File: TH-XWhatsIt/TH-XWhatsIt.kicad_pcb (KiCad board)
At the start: 2 copper layers, 178 x 115.5 mm, 42 parts, among them J1 COLUMNS, J10 DISPLAYWRITER PLUGBOARD CONNE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, J11 DISPLAYWRITER PLUGBOARD ROWS, J12 EXPANSION HEADER, J2 ROWS, J3 MODEL F PLUGBOARD COLUMNS, J4 MODEL F PLUGBOARD CONNECTOR, J5 MODEL F PLUGBOARD ROWS, J6 BEAMSPRING PLUGBOARD COLUMNS, J7 BEAMSPRING PLUGBOARD CONNECTOR, J8 BEAMSPRING PLUGBOARD ROWS, J9 DISPLAYWRITER PLUGBOARD COLUM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, U1 LM339, U2 MCP4921-EP, U3 74HCT595, U5 74HCT595, U6 LM339, U7 ProMicro, U8 74HCT595

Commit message: My try of adding model-f at support
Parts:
- removed C2: 10U, Capacitor_THT:C_Disc_D3.0mm_W1.6mm_P2.50mm
- removed H2: GROUND STRAP, MountingHole:MountingHole_2.2mm_M2_Pad_Via
- removed J11: DISPLAYWRITER PLUGBOARD ROWS, Connector_PinSocket_2.54mm:PinSocket_1x12_P2.54mm_Vertical
- removed J4: MODEL F PLUGBOARD CONNECTOR, Connector_PinHeader_2.54mm:PinHeader_1x30_P2.54mm_Horizontal
- removed J5: MODEL F PLUGBOARD ROWS, Connector_PinSocket_2.54mm:PinSocket_1x12_P2.54mm_Vertical
- removed J6: BEAMSPRING PLUGBOARD COLUMNS, Connector_PinSocket_2.54mm:PinSocket_1x27_P2.54mm_Vertical
- removed J8: BEAMSPRING PLUGBOARD ROWS, Connector_PinSocket_2.54mm:PinSocket_1x12_P2.54mm_Vertical
- removed J9: DISPLAYWRITER PLUGBOARD COLUMNS, Connector_PinSocket_2.54mm:PinSocket_1x27_P2.54mm_Vertical
- removed R6: 4K7, Resistor_THT:R_Axial_DIN0204_L3.6mm_D1.6mm_P1.90mm_Vertical
- removed R7: 1K, Resistor_THT:R_Axial_DIN0204_L3.6mm_D1.6mm_P1.90mm_Vertical
- added H10: GROUND STRAP, MountingHole:MountingHole_4.5mm_Pad, F.Cu at (225.6, 149.3)
- added J13: Conn_01x30, TH-XWhatsIt:SIP-30-P3.96, F.Cu at (159.3, 150.2)
- added J22: Conn_01x08, Connector_PinSocket_2.54mm:PinSocket_1x08_P2.54mm_Vertical, F.Cu at (149.4, 139.1)
- added J44: MODEL F PLUGBOARD CONNECTOR, Connector_PinHeader_2.54mm:PinHeader_1x30_P2.54mm_Horizontal, B.Cu at (124.0, 146.1)
- H1, H3, H4: footprint MountingHole:MountingHole_2.2mm_M2_Pad_Via -> MountingHole:MountingHole_3.2mm_M3_Pad
- J1: value COLUMNS -> Conn_01x08; footprint Connector_PinHeader_2.54mm:PinHeader_1x27_P2.54mm_Vertical -> Connector_PinSocket_2.54mm:PinSocket_1x08_P2.54mm_Vertical; moved to B.Cu
- J2: value ROWS -> MODEL F PLUGBOARD CONNECTOR; footprint Connector_PinHeader_2.54mm:PinHeader_1x12_P2.54mm_Vertical -> Connector_PinHeader_2.54mm:PinHeader_1x30_P2.54mm_Vertical; moved to B.Cu
- J3: value MODEL F PLUGBOARD COLUMNS -> MODEL F PLUGBOARD CONNECTOR; footprint Connector_PinSocket_2.54mm:PinSocket_1x27_P2.54mm_Vertical -> Connector_PinHeader_2.54mm:PinHeader_1x30_P2.54mm_Vertical; moved to F.Cu
- moved J2 100.0 mm to (124.0, 116.7)
- moved J1 69.6 mm to (149.4, 109.1), turned to 270 degrees
- moved J3 44.4 mm to (123.9, 87.3), turned to 90 degrees
- moved R1 9.41 mm to (225.3, 133.7)
- moved RN3 8.68 mm to (198.1, 138.9), turned to 180 degrees
- moved C10 8.34 mm to (204.8, 124.6), turned to 180 degrees
- moved R2 7.66 mm to (228.0, 135.6), turned to 90 degrees
- moved RN1 7.66 mm to (217.2, 138.8)
- moved C4 5.85 mm to (166.7, 126.3)
- moved C3 5.69 mm to (166.7, 132.3)
- moved U2 5.58 mm to (170.6, 134.3)
- moved C7 5.45 mm to (136.8, 132.1)
- moved U8 5.39 mm to (140.4, 134.7)
- moved C5 5.38 mm to (111.7, 132.1)
- moved U3 5.37 mm to (90.2, 134.6)
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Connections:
- J1 pad 1: GNDA -> /beamspring plugboard/BSCOL17
- J1 pad 2: GNDA -> /beamspring plugboard/BSCOL18
- J1 pad 3: COL1 -> /beamspring plugboard/BSCOL19
- J1 pad 4: COL2 -> /beamspring plugboard/BSCOL20
- J1 pad 5: COL3 -> /beamspring plugboard/BSCOL21
- J1 pad 6: COL4 -> /beamspring plugboard/BSCOL22
- J1 pad 7: COL5 -> /beamspring plugboard/BSCOL23
- J1 pad 8: COL6 -> /beamspring plugboard/BSGROUND
- J2 pad 1: GNDA -> /beamspring plugboard/BSGROUND
- J2 pad 10: SENSE8 -> /beamspring plugboard/BSCOL8
- J2 pad 11: GNDA -> /beamspring plugboard/BSCOL9
- J2 pad 12: GNDA -> /beamspring plugboard/BSCOL10
- J2 pad 2: GNDA -> /beamspring plugboard/BSGROUND
- J2 pad 3: SENSE1 -> /beamspring plugboard/BSCOL1
- J2 pad 4: SENSE2 -> /beamspring plugboard/BSCOL2
- J2 pad 5: SENSE3 -> /beamspring plugboard/BSCOL3
- J2 pad 6: SENSE4 -> /beamspring plugboard/BSCOL4
- J2 pad 7: SENSE5 -> /beamspring plugboard/BSCOL5
- J2 pad 8: SENSE7 -> /beamspring plugboard/BSCOL6
- J2 pad 9: SENSE6 -> /beamspring plugboard/BSCOL7
- J3 pad 1: /model f plugboard/MFGROUND -> /displaywriter plugboard/DWGROUND
- J3 pad 10: /model f plugboard/MFCOL8 -> /displaywriter plugboard/DWCOL8
- J3 pad 11: /model f plugboard/MFCOL9 -> /displaywriter plugboard/DWCOL9
- J3 pad 12: /model f plugboard/MFCOL10 -> /displaywriter plugboard/DWCOL10
- J3 pad 13: /model f plugboard/MFCOL11 -> /displaywriter plugboard/DWCOL11
- J3 pad 14: /model f plugboard/MFCOL12 -> /displaywriter plugboard/DWCOL12
- J3 pad 15: /model f plugboard/MFCOL13 -> (no net)
- J3 pad 16: /model f plugboard/MFCOL14 -> (no net)
- J3 pad 17: /model f plugboard/MFCOL15 -> (no net)
- J3 pad 18: /model f plugboard/MFCOL16 -> (no net)
- J3 pad 19: (no net) -> /displaywriter plugboard/DWGROUND
- J3 pad 2: /model f plugboard/MFGROUND -> /displaywriter plugboard/DWGROUND
- J3 pad 20: (no net) -> /displaywriter plugboard/DWGROUND
- J3 pad 21: (no net) -> /displaywriter plugboard/DWSENSE1
- J3 pad 22: (no net) -> /displaywriter plugboard/DWSENSE2
- J3 pad 23: (no net) -> /displaywriter plugboard/DWSENSE3
- J3 pad 24: (no net) -> /displaywriter plugboard/DWSENSE4
- J3 pad 25: (no net) -> /displaywriter plugboard/DWSENSE8
- J3 pad 26: /model f plugboard/MFGROUND -> /displaywriter plugboard/DWSENSE7
- J3 pad 27: /model f plugboard/MFGROUND -> /displaywriter plugboard/DWSENSE6
- J3 pad 3: /model f plugboard/MFCOL1 -> /displaywriter plugboard/DWCOL1
- J3 pad 4: /model f plugboard/MFCOL2 -> /displaywriter plugboard/DWCOL2
- J3 pad 5: /model f plugboard/MFCOL3 -> /displaywriter plugboard/DWCOL3
- J3 pad 6: /model f plugboard/MFCOL4 -> /displaywriter plugboard/DWCOL4
- J3 pad 7: /model f plugboard/MFCOL5 -> /displaywriter plugboard/DWCOL5
- J3 pad 8: /model f plugboard/MFCOL6 -> /displaywriter plugboard/DWCOL6
- J3 pad 9: /model f plugboard/MFCOL7 -> /displaywriter plugboard/DWCOL7
- RN3 pad 1: Net-(R6-Pad2) -> Net-(R1-Pad2)
- RN3 pad 2: SENSE8 -> SENSE5
- RN3 pad 3: SENSE6 -> SENSE7
- RN3 pad 4: SENSE7 -> SENSE6
- RN3 pad 5: SENSE5 -> SENSE8
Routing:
- net /model f plugboard/MFGROUND: track 318.4 -> 0.00 mm
- net +5VA: track 517.5 -> 414.4 mm, vias 2 -> 0
- net COL1: track 18.9 -> 75.3 mm
- net COL2: track 9.81 -> 65.7 mm
- net COL3: track 9.25 -> 64.3 mm
- net COL4: track 9.25 -> 62.9 mm
- net COL5: track 9.25 -> 61.4 mm
- net /model f plugboard/MFSENSE1: track 52.1 -> 0.00 mm
- net /model f plugboard/MFSENSE8: track 51.1 -> 0.00 mm
- net /model f plugboard/MFSENSE6: track 51.1 -> 0.00 mm
- net /model f plugboard/MFSENSE3: track 51.1 -> 0.00 mm
- net /model f plugboard/MFSENSE7: track 51.1 -> 0.00 mm
- net /model f plugboard/MFSENSE5: track 51.1 -> 0.00 mm
- net /model f plugboard/MFSENSE4: track 51.1 -> 0.00 mm
- net /model f plugboard/MFSENSE2: track 51.1 -> 0.00 mm
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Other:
- board size 178 x 115.5 mm -> 178 x 93.7 mm

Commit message: move stuff around near sense lines
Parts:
- moved C10 23.2 mm to (186.9, 139.4), turned to 0 degrees
- moved C9 21.0 mm to (208.8, 139.5)
- moved RN1 4.69 mm to (221.9, 139.2)
- moved RN3 4.67 mm to (202.8, 139.0)
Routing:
- net GNDA: track 488.8 -> 459.9 mm, vias 5 -> 3
- net Net-(R1-Pad2): track 52.4 -> 59.6 mm, vias 2 -> 1
- net SENSE3: track 55.3 -> 58.4 mm
- net SENSE6: track 40.8 -> 43.8 mm
- net SETPOINT: track 87.5 -> 90.0 mm, vias 1 -> 0
- net SENSE4: track 52.8 -> 55.2 mm
- net SENSE8: track 38.4 -> 40.7 mm
- net SENSE2: track 47.6 -> 49.4 mm
- net SENSE7: track 33.1 -> 34.8 mm
- net SENSE1: track 52.7 -> 51.8 mm

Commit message: some more small fixes
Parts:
- J13: value Conn_01x30 -> Model F AT
- J22: value Conn_01x08 -> Beamsring extra
- J44: value MODEL F PLUGBOARD CONNECTOR -> Model F or Plugboard
- U7: footprint promicro:ProMicro -> TH-XWhatsIt:ProMicro
- moved C10 2.52 mm to (189.4, 139.4), turned to 180 degrees
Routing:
- net +5VA: track 414.5 -> 415.6 mm
- net GNDA: track 459.9 -> 459.6 mm, vias 3 -> 1

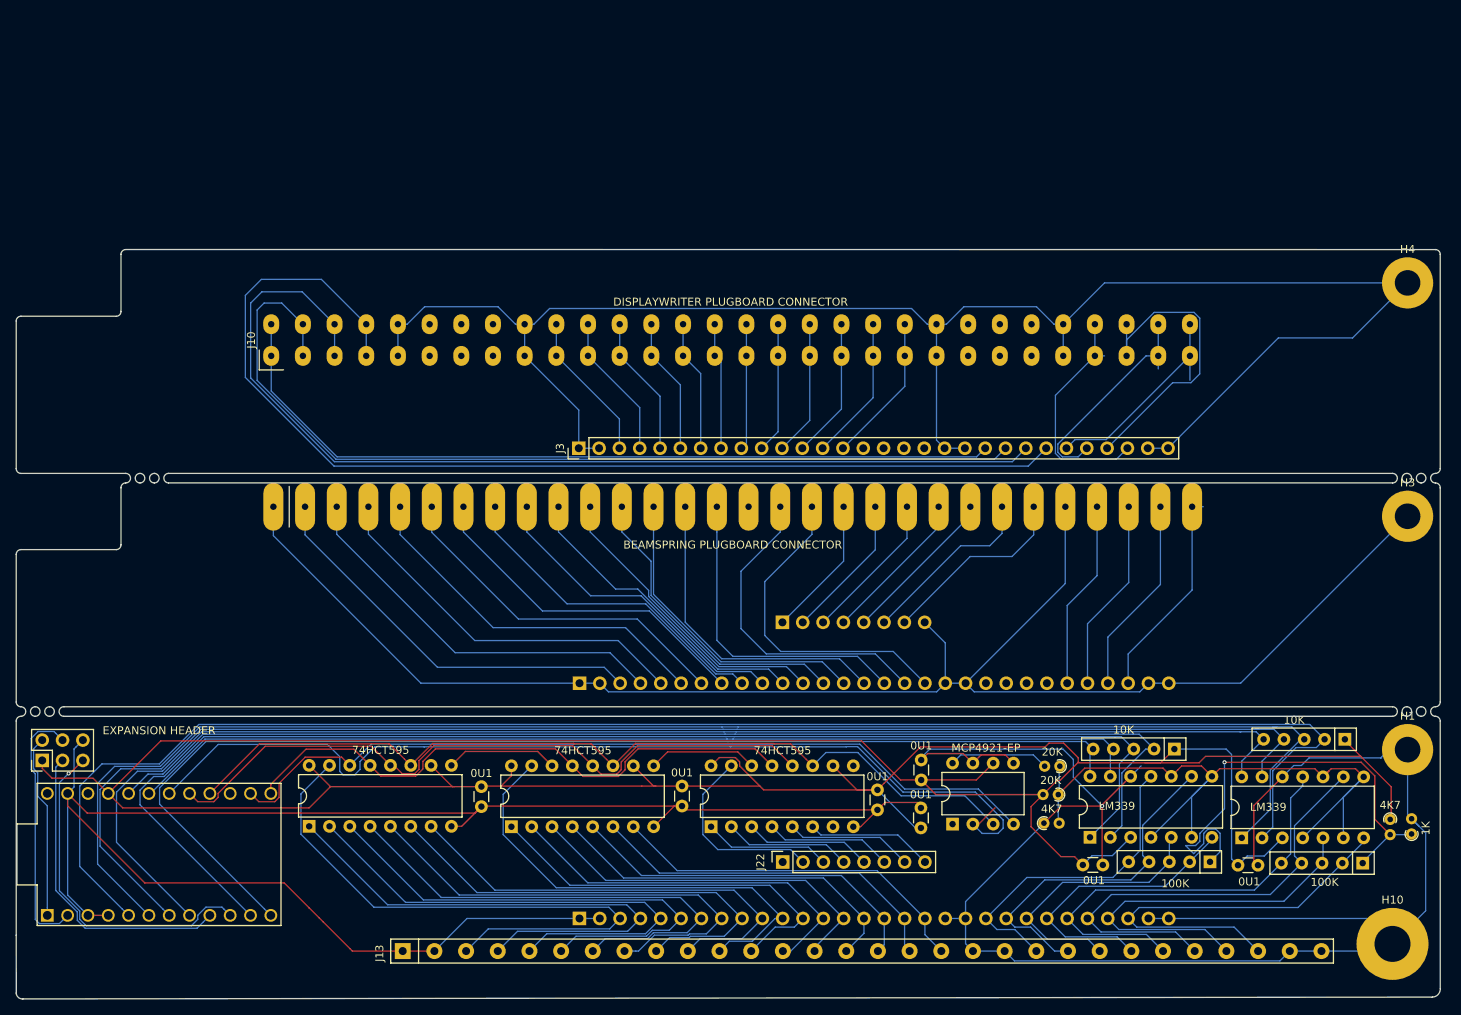
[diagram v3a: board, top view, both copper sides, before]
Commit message: fix drc and unconnected networks
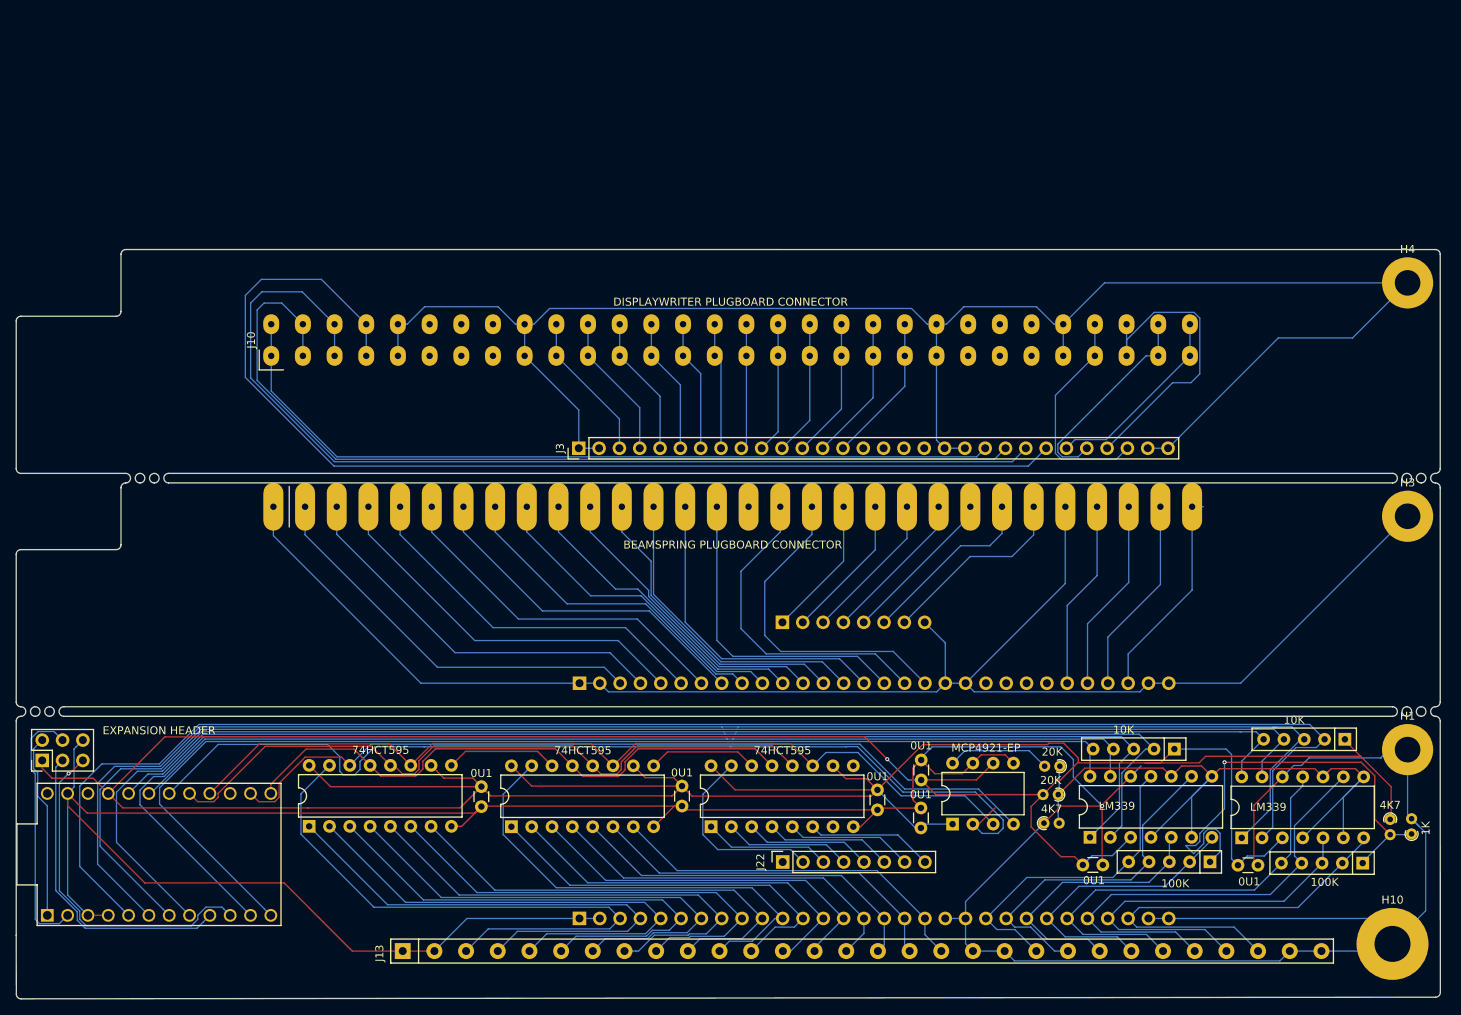
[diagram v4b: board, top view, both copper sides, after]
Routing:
- net +5VA: track 415.6 -> 480.4 mm, vias 0 -> 1
- net GNDA: track 459.6 -> 466.8 mm
- net /displaywriter plugboard/DWSENSE8: track 27.2 -> 24.2 mm
- net /displaywriter plugboard/DWSENSE7: track 28.0 -> 26.4 mm
- net /displaywriter plugboard/DWSENSE5: track 29.3 -> 28.1 mm
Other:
- outline, holes or cut-outs redrawn
